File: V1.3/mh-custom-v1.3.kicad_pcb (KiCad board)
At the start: 2 copper layers, 97 x 91.3 mm, 121 parts, among them J1 Conn_01x03_Male, J10 Screw_Terminal_01x02, J11 Screw_Terminal_01x02, J12 Screw_Terminal_01x02, J13 USB_A, J14 Screw_Terminal_01x02, J3 Conn_02x19_Top_Bottom, J4 Conn_02x19_Top_Bottom, J5 Screw_Terminal_01x02, J6 Screw_Terminal_01x02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

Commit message: added stage levels to Estops on F.Silkscreen
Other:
- board text added: "POWER"
- board text added: "stage 1"
- board text added: "stage 2"
- board text removed: "PWR"
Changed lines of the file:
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@@
     (effects (font (size 2 2) (thickness 0.3)))
+  )
+  (gr_text "stage 1 " (at 129.025 48.6 90) (layer "F.SilkS")
+    (effects (font (size 1 1) (thickness 0.15)))
   )
   (gr_text "Set DIP switches\nfor board config \n" (at 48.0906 32.855) (layer "F.SilkS")
@@
   (gr_text "OUT" (at 127.14 88.9 90) (layer "F.SilkS")
     (effects (font (size 2.5 2.5) (thickness 0.5)))
+  )
+  (gr_text "stage 2 " (at 129.025 98.8 90) (layer "F.SilkS")
+    (effects (font (size 1 1) (thickness 0.15)))
   )
   (gr_text "R.btn" (at 127.08 58.819999 90) (layer "F.SilkS")
@@
   )
   (gr_text "5V|GND" (at 78.685 96.09) (layer "F.SilkS")
+    (effects (font (size 1 1) (thickness 0.15)))
+  )
+  (gr_text "stage 2 " (at 129.025 108.6 90) (layer "F.SilkS")
     (effects (font (size 1 1) (thickness 0.15)))
   )
@@
     (effects (font (size 2 2) (thickness 0.3)))
   )
-  (gr_text "PWR" (at 79.828 111.2208 90) (layer "F.SilkS")
-    (effects (font (size 1 1) (thickness 0.2)))
+  (gr_text "POWER" (at 80.025 112.8 90) (layer "F.SilkS")
+    (effects (font (size 1 1) (thickness 0.2)) (justify left))
   )
   (gr_text "Bypass\nKey\nInput" (at 82.015 32.19 180) (layer "F.SilkS")
@@
     (effects (font (size 1 1) (thickness 0.15)))
   )
+  (gr_text "stage 1 " (at 129.025 38.8 90) (layer "F.SilkS")
+    (effects (font (size 1 1) (thickness 0.15)))
+  )

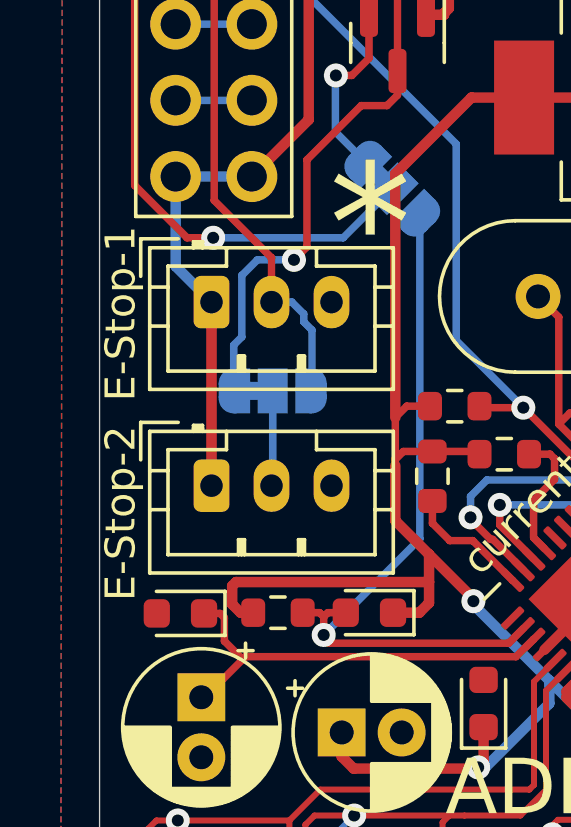
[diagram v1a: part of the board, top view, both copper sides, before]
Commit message: made EStop Header labels more readable
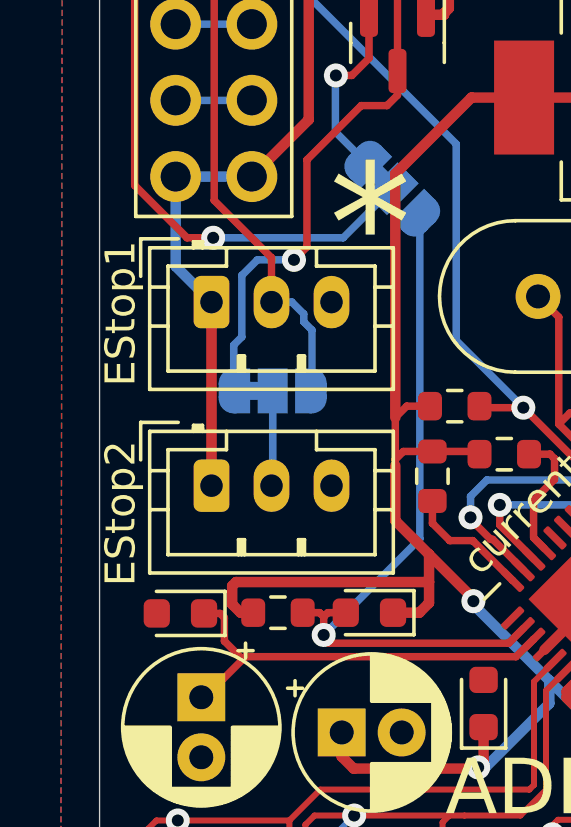
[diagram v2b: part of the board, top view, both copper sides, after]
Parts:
- renumbered E-Stop-1 to EStop1, E-Stop-2 to EStop2
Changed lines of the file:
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@@
     (property "Sheetname" "lightsounds")
     (attr through_hole)
-    (fp_text reference "E-Stop-2" (at -3.03 0.9208 270) (layer "F.SilkS")
+    (fp_text reference "EStop2" (at -3.03 0.9208 270) (layer "F.SilkS")
       (effects (font (size 1 1) (thickness 0.15)))
     )
@@
     (property "Sheetname" "lightsounds")
     (attr through_hole)
-    (fp_text reference "E-Stop-1" (at -3.03 0.38 90) (layer "F.SilkS")
-      (effects (font (size 1 1) (thickness 0.15)))
-    )
+    (fp_text reference "EStop1" (at -3.03 0.38 90) (layer "F.SilkS")
+      (effects (font (size 1 1) (thickness 0.15)))
+    )

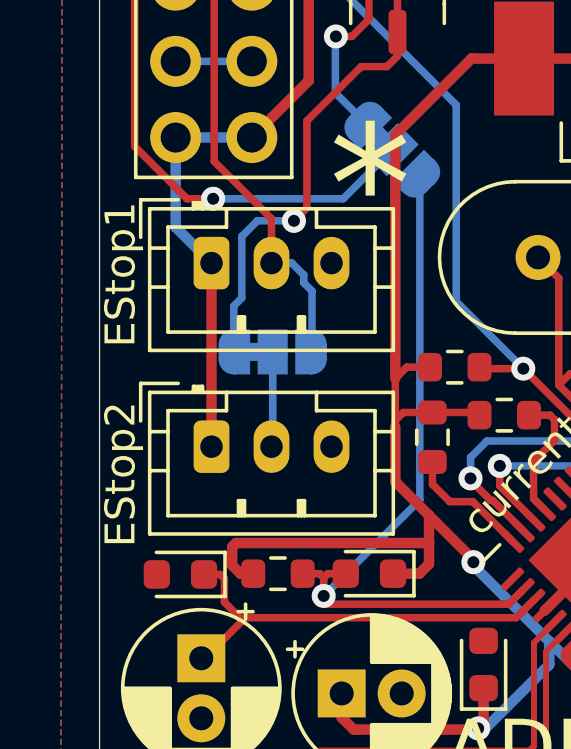
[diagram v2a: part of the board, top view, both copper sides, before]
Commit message: change silkscreen lables for the E-Stop JST connectors, to match large-gauge wiring
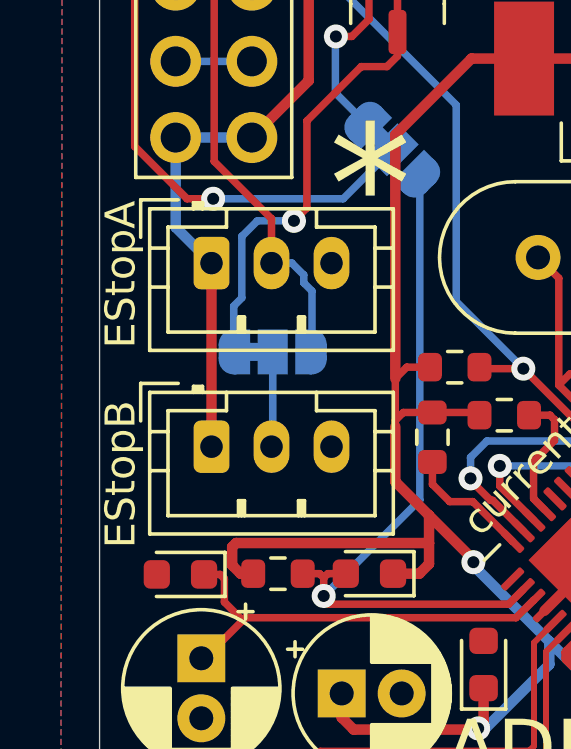
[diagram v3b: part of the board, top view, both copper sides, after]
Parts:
- renumbered EStop1 to EStopA, EStop2 to EStopB
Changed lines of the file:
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@@
     (property "Sheetname" "lightsounds")
     (attr through_hole)
-    (fp_text reference "EStop2" (at -3.03 0.9208 270) (layer "F.SilkS")
+    (fp_text reference "EStopB" (at -3.03 0.9208 270) (layer "F.SilkS")
       (effects (font (size 1 1) (thickness 0.15)))
     )
@@
     (property "Sheetname" "lightsounds")
     (attr through_hole)
-    (fp_text reference "EStop1" (at -3.03 0.38 90) (layer "F.SilkS")
-      (effects (font (size 1 1) (thickness 0.15)))
-    )
+    (fp_text reference "EStopA" (at -3.03 0.38 90) (layer "F.SilkS")
+      (effects (font (size 1 1) (thickness 0.15)))
+    )

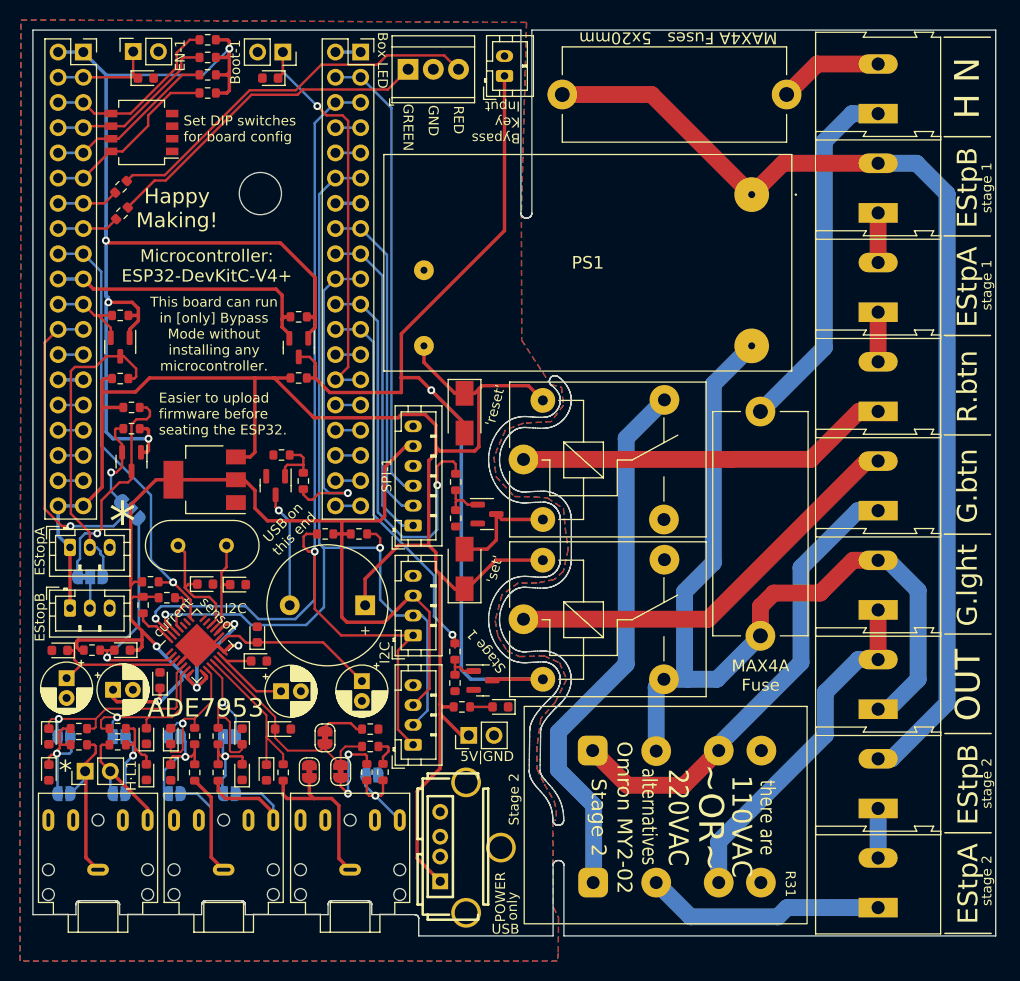
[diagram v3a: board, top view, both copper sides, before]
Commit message: fixes to board, based on Iris' feedback
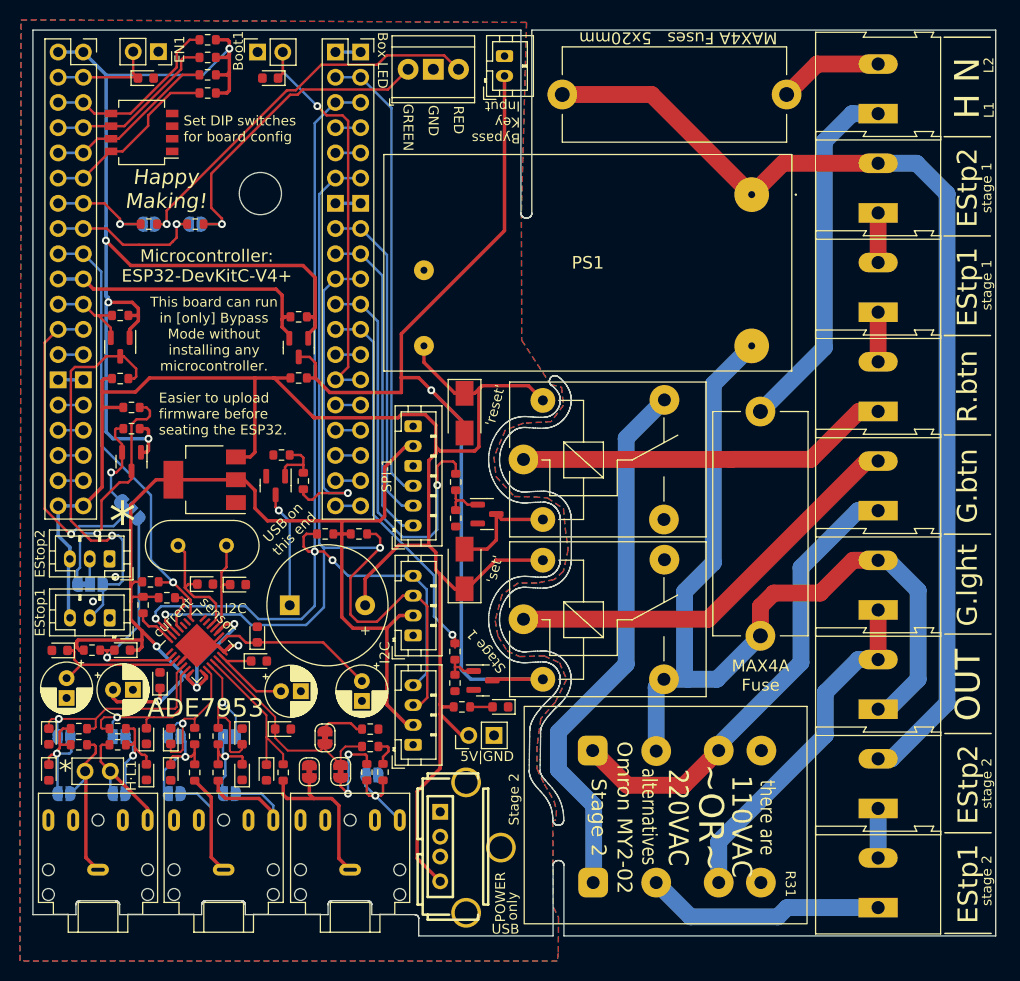
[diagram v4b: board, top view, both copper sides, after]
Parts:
- removed Boot-1, EN-1: Conn_01x02_Female, Connector_PinSocket_2.54mm:PinSocket_1x02_P2.54mm_Vertical
- removed EStopA, EStopB: Conn_01x03_Female, Connector_JST:JST_PH_B3B-PH-K_1x03_P2.00mm_Vertical
- added Boot1: Conn_01x02_Female, Connector_PinSocket_2.54mm:PinSocket_1x02_P2.54mm_Vertical, F.Cu at (55.6, 25.1)
- added EN1: Conn_01x02_Female, Connector_PinSocket_2.54mm:PinSocket_1x02_P2.54mm_Vertical, F.Cu at (45.6, 25.1)
- added EStop1: Conn_01x03_Female, Connector_JST:JST_PH_B3B-PH-K_1x03_P2.00mm_Vertical, F.Cu at (40.7, 82.1)
- added EStop2: Conn_01x03_Female, Connector_JST:JST_PH_B3B-PH-K_1x03_P2.00mm_Vertical, F.Cu at (40.6, 76.2)
- added JP15: no-filter-1, Jumper:SolderJumper-2_P1.3mm_Open_RoundedPad1.0x1.5mm, B.Cu at (44.6, 42.5)
- added JP16: no-filter-1, Jumper:SolderJumper-2_P1.3mm_Open_RoundedPad1.0x1.5mm, B.Cu at (49.3, 42.5)
- moved R6 7.47 mm to (49.3, 42.5), turned to 180 degrees
- moved R5 4.69 mm to (44.6, 42.5), turned to 0 degrees
- moved JP14 0.76 mm to (38.7, 78.8)
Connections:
- I2C-2 pad 1: SCL -> GND
- I2C-2 pad 2: SDA -> +3.3V
- I2C-2 pad 3: +3.3V -> SDA
- I2C-2 pad 4: GND -> SCL
- I2C-3 pad 1: SCL -> GND
- I2C-3 pad 2: SDA -> +3.3V
- I2C-3 pad 3: +3.3V -> SDA
- I2C-3 pad 4: GND -> SCL
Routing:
- net led-grn: track 6.25 -> 16.6 mm, vias 0 -> 1
- net Net-(EStop1-Pad2): track 31.9 -> 41.1 mm, vias 0 -> 1
- net SDA: track 96.2 -> 102.9 mm
- net led-red: track 6.20 -> 11.8 mm, vias 0 -> 1
- net SCL: track 107.2 -> 101.6 mm, vias 2 -> 3
- net +3.3V: track 132.2 -> 130.9 mm
- net +5V: track 181.6 -> 182.7 mm
- net Net-(JP14-Pad1): track 22.7 -> 23.5 mm
- net Net-(J1-Pad3): track 39.5 -> 40.1 mm, vias 0 -> 1
- net two-options: track 31.2 -> 31.9 mm
- net Net-(EStop2-Pad2): track 3.18 -> 2.58 mm
- net Net-(J1-Pad1): track 34.0 -> 33.6 mm, vias 0 -> 1
- net GND: vias 1 -> 3
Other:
- board text added: "EStp1"
- board text added: "EStp2"
- board text added: "L1"
- board text added: "L2"
- board text removed: "EStpA"
- board text removed: "EStpB"
